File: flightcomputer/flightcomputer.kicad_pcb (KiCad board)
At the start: 2 copper layers, 112 x 120 mm, 0 parts

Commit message: all boards
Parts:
- added BZ1: Buzzer, Buzzer_Beeper:MagneticBuzzer_PUI_AT-0927-TT-6-R, F.Cu at (162.8, 84.8)
- added C1: 0.1uF, Capacitor_SMD:C_0402_1005Metric_Pad0.74x0.62mm_HandSolder, F.Cu at (152.9, 93.3)
- added C10: 10uF, Capacitor_SMD:C_0603_1608Metric_Pad1.08x0.95mm_HandSolder, F.Cu at (163.2, 134.0)
- added C11: 10uF, Capacitor_SMD:C_0603_1608Metric_Pad1.08x0.95mm_HandSolder, F.Cu at (137.9, 98.0)
- added C2: 220nF, Capacitor_SMD:C_0402_1005Metric_Pad0.74x0.62mm_HandSolder, F.Cu at (152.9, 95.2)
- added C3: 0.1uF, Capacitor_SMD:C_0402_1005Metric_Pad0.74x0.62mm_HandSolder, F.Cu at (152.9, 97.2)
- added C4: 100nF, Capacitor_SMD:C_0402_1005Metric_Pad0.74x0.62mm_HandSolder, F.Cu at (152.9, 99.2)
- added C5: 0.1uF, Capacitor_SMD:C_0402_1005Metric_Pad0.74x0.62mm_HandSolder, F.Cu at (152.9, 101.2)
- added C6: 10uF, Capacitor_SMD:C_0402_1005Metric_Pad0.74x0.62mm_HandSolder, F.Cu at (152.9, 103.1)
- added C7: 10uF, Capacitor_SMD:C_0603_1608Metric_Pad1.08x0.95mm_HandSolder, F.Cu at (137.9, 90.5)
- added C8: 22uF, Capacitor_SMD:C_0603_1608Metric_Pad1.08x0.95mm_HandSolder, F.Cu at (137.9, 93.0)
- added C9: 100nF, Capacitor_SMD:C_0603_1608Metric_Pad1.08x0.95mm_HandSolder, F.Cu at (137.9, 95.5)
- added D1: LED, LED_SMD:LED_0603_1608Metric_Pad1.05x0.95mm_HandSolder, F.Cu at (171.6, 91.4)
- added D2: LED, LED_SMD:LED_0603_1608Metric_Pad1.05x0.95mm_HandSolder, F.Cu at (171.6, 94.0)
- added D3: LED, LED_SMD:LED_0603_1608Metric_Pad1.05x0.95mm_HandSolder, F.Cu at (171.6, 96.6)
- added H1: MountingHole_Pad, MountingHole:MountingHole_2.2mm_M2_DIN965_Pad, F.Cu at (113.6, 82.2)
- added H2: MountingHole_Pad, MountingHole:MountingHole_2.2mm_M2_DIN965_Pad, F.Cu at (113.6, 87.6)
- added H3: MountingHole_Pad, MountingHole:MountingHole_2.2mm_M2_DIN965_Pad, F.Cu at (113.6, 92.9)
- added H4: MountingHole_Pad, MountingHole:MountingHole_2.2mm_M2_DIN965_Pad, F.Cu at (113.6, 98.3)
- added J1: Conn_Coaxial, Connector_Coaxial:U.FL_Hirose_U.FL-R-SMT-1_Vertical, F.Cu at (163.6, 143.3)
- added J10: Conn_01x03, Connector_PinHeader_2.54mm:PinHeader_1x03_P2.54mm_Vertical, F.Cu at (135.0, 81.9)
- added J11: Conn_01x03, Connector_PinHeader_2.54mm:PinHeader_1x03_P2.54mm_Vertical, F.Cu at (139.6, 81.9)
- added J12: 282837-2, HPRfootprints:TE_282837-2, F.Cu at (122.2, 84.4)
- added J13: 282837-2, HPRfootprints:TE_282837-2, F.Cu at (122.2, 94.2)
- added J2: Conn_Coaxial, Connector_Coaxial:SMA_Amphenol_132134-10_Vertical, F.Cu at (143.6, 119.8)
- added J3: Conn_Coaxial, Connector_Coaxial:U.FL_Hirose_U.FL-R-SMT-1_Vertical, F.Cu at (169.0, 143.3)
- added J4: Conn_Coaxial, Connector_Coaxial:SMA_Amphenol_132134-10_Vertical, F.Cu at (143.6, 129.0)
- added J5: Conn_01x24, Connector_Molex:Molex_SL_171971-0024_1x24_P2.54mm_Vertical, F.Cu at (3.02, 3.08)
- added J6: Conn_01x24, Connector_Molex:Molex_SL_171971-0024_1x24_P2.54mm_Vertical, F.Cu at (3.02, 11.7)
- added J7: Conn_01x01, Connector_PinHeader_2.54mm:PinHeader_1x01_P2.54mm_Vertical, F.Cu at (130.3, 81.9)
- added J8: Conn_01x01, Connector_PinHeader_2.54mm:PinHeader_1x01_P2.54mm_Vertical, F.Cu at (130.3, 86.5)
- added J9: Conn_01x02, Connector_JST:JST_PH_S2B-PH-K_1x02_P2.00mm_Horizontal, F.Cu at (162.5, 100.8)
- added M1: Motor_Servo, Connector_PinHeader_2.54mm:PinHeader_1x03_P2.54mm_Vertical, F.Cu at (144.3, 81.9)
- added M2: Motor_Servo, Connector_PinHeader_2.54mm:PinHeader_1x03_P2.54mm_Vertical, F.Cu at (148.9, 81.9)
- added Q1: MMBT3904, Package_TO_SOT_SMD:SOT-23, F.Cu at (172.5, 81.9)
- added Q2: MMBT3904, Package_TO_SOT_SMD:SOT-23, F.Cu at (172.5, 86.6)
- added Q3: SI4925DDY-T1-GE3, HPRfootprints:SOIC127P600X175-8N, F.Cu at (120.5, 102.3)
- added R1: 4.7k, Resistor_SMD:R_0603_1608Metric_Pad0.98x0.95mm_HandSolder, F.Cu at (163.2, 136.5)
- added R10: 150, Resistor_SMD:R_0603_1608Metric_Pad0.98x0.95mm_HandSolder, F.Cu at (146.6, 93.0)
- added R11: 150, Resistor_SMD:R_0603_1608Metric_Pad0.98x0.95mm_HandSolder, F.Cu at (146.6, 95.5)
- added R2: 4.7k, Resistor_SMD:R_0603_1608Metric_Pad0.98x0.95mm_HandSolder, F.Cu at (163.2, 139.0)
- added R3: 1.2k, Resistor_SMD:R_0603_1608Metric_Pad0.98x0.95mm_HandSolder, F.Cu at (137.9, 100.5)
- added R4: 4.7k, Resistor_SMD:R_0603_1608Metric_Pad0.98x0.95mm_HandSolder, F.Cu at (142.2, 90.5)
- added R5: 1K, Resistor_SMD:R_0603_1608Metric_Pad0.98x0.95mm_HandSolder, F.Cu at (142.2, 93.0)
- added R6: 1K, Resistor_SMD:R_0603_1608Metric_Pad0.98x0.95mm_HandSolder, F.Cu at (142.2, 95.5)
- added R7: 10K, Resistor_SMD:R_0603_1608Metric_Pad0.98x0.95mm_HandSolder, F.Cu at (142.2, 98.0)
- added R8: 10K, Resistor_SMD:R_0603_1608Metric_Pad0.98x0.95mm_HandSolder, F.Cu at (142.2, 100.5)
- added R9: 150, Resistor_SMD:R_0603_1608Metric_Pad0.98x0.95mm_HandSolder, F.Cu at (146.6, 90.5)
- added S1: KMR221GLFS, HPRfootprints:SW_KMR221GLFS, F.Cu at (170.7, 100.9)
- added S2: KMR221GLFS, HPRfootprints:SW_KMR221GLFS, F.Cu at (170.7, 105.5)
- added TP1: TestPoint, Connector_PinHeader_2.54mm:PinHeader_1x01_P2.54mm_Vertical, F.Cu at (130.3, 91.2)
- added TP2: TestPoint, Connector_PinHeader_2.54mm:PinHeader_1x01_P2.54mm_Vertical, F.Cu at (130.3, 95.8)
- added TP3: TestPoint, TestPoint:TestPoint_Pad_1.0x1.0mm, F.Cu at (134.2, 90.8)
- added TP4: TestPoint, TestPoint:TestPoint_Pad_1.0x1.0mm, F.Cu at (134.2, 93.8)
- added TP5: TestPoint, TestPoint:TestPoint_Pad_1.0x1.0mm, F.Cu at (134.2, 96.9)
- added TP6: TestPoint, TestPoint:TestPoint_Pad_1.0x1.0mm, F.Cu at (134.2, 99.9)
- added TP7: TestPoint, TestPoint:TestPoint_Pad_1.0x1.0mm, F.Cu at (134.2, 103.0)
- added U1: MAX-M10S, RF_GPS:ublox_MAX, F.Cu at (154.7, 138.7)
- added U2: LIS2MDLTR, HPRfootprints:PQFN50P200X200X70-12N, F.Cu at (144.2, 103.6)
- added U3: BMI088, HPRfootprints:PQFN50P450X300X100-16N, F.Cu at (138.9, 104.6)
- added U4: MS5607-02BA, Package_LGA:LGA-8_3x5mm_P1.25mm, F.Cu at (156.9, 95.8)
- added U5: MIC29302AWD-TR, HPRfootprints:TO-252-5_MCH, F.Cu at (155.4, 85.2)
- added U6: RFM95W-915S2, RF_Module:HOPERF_RFM9XW_SMD, F.Cu at (158.0, 124.0)
- added U7: Teensy4.1, HPRfootprints:Teensy41, F.Cu at (147.5, 64.5)
- added U8: LD1117S50TR_SOT223, Package_TO_SOT_SMD:SOT-223-3_TabPin2, F.Cu at (164.4, 94.3)

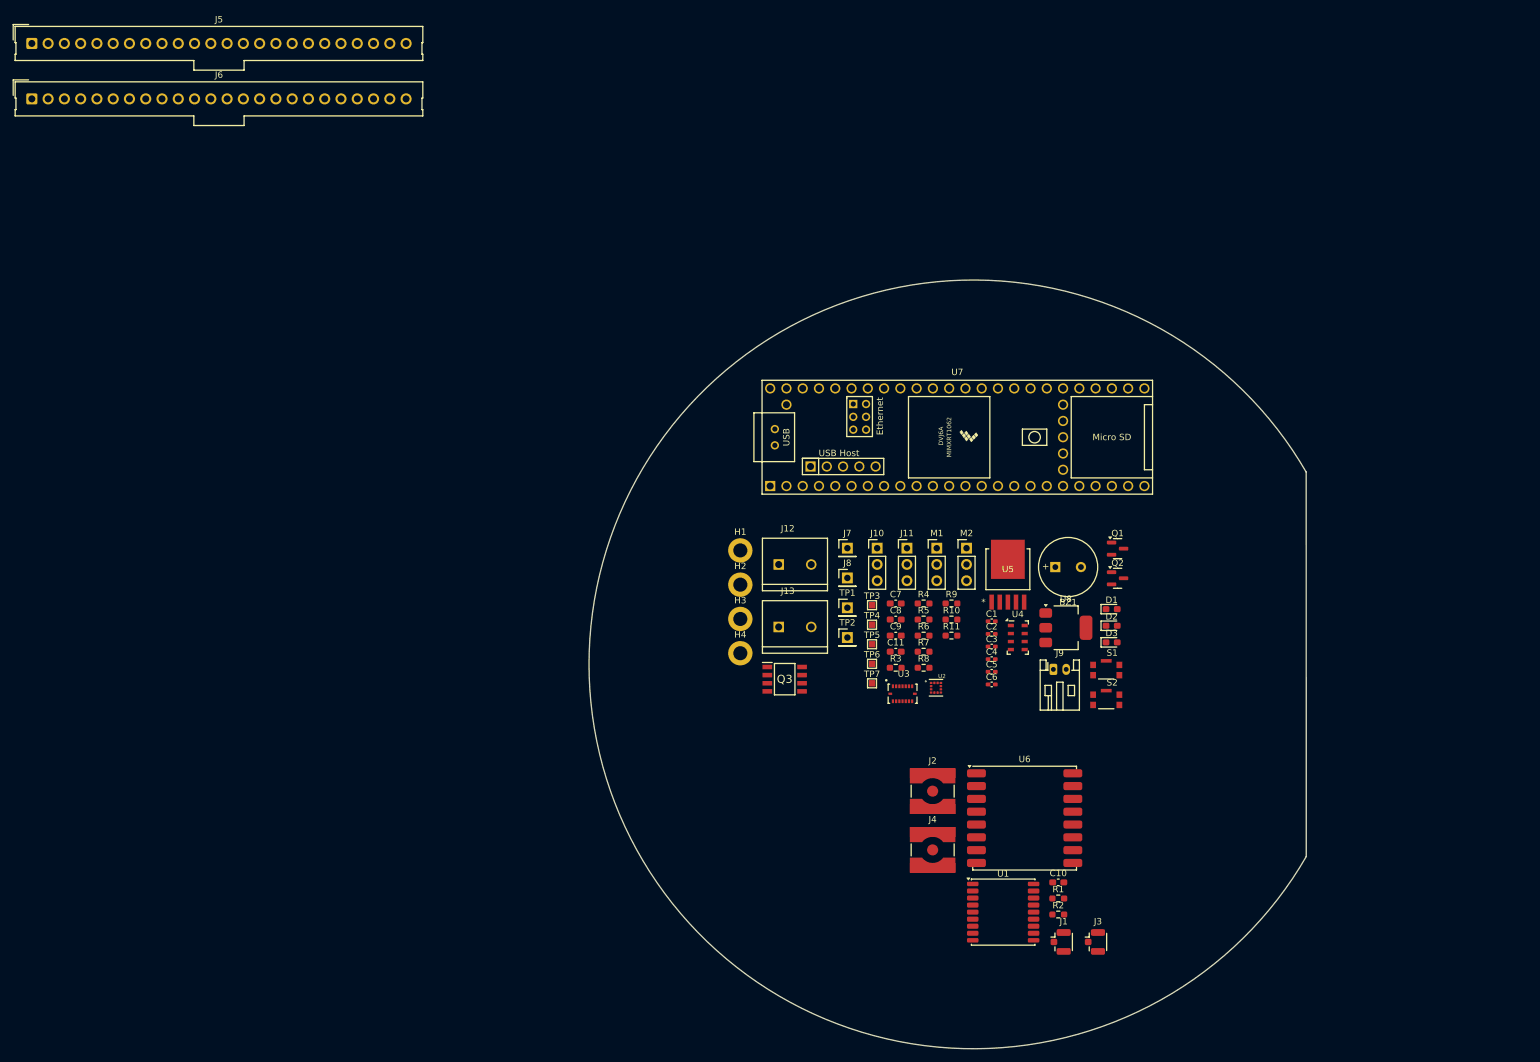
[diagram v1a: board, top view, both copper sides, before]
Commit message: no esp32, may add
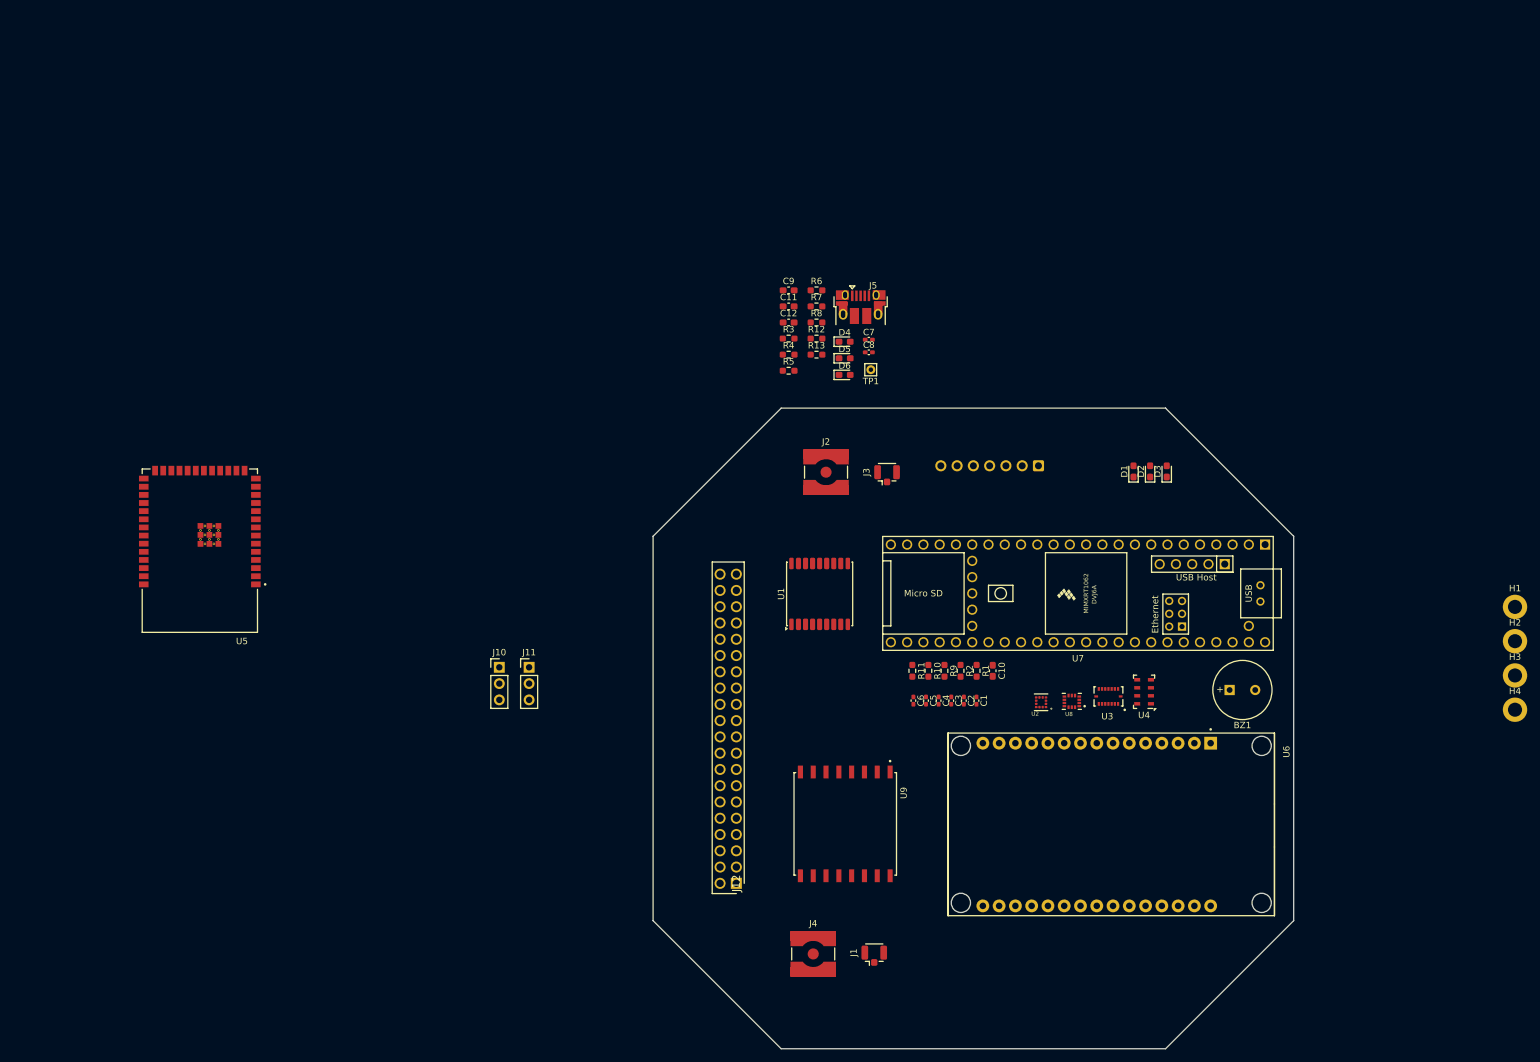
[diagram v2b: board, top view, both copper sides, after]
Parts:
- removed J6: Conn_01x24, Connector_Molex:Molex_SL_171971-0024_1x24_P2.54mm_Vertical
- removed J7, J8: Conn_01x01, Connector_PinHeader_2.54mm:PinHeader_1x01_P2.54mm_Vertical
- removed J9: Conn_01x02, Connector_JST:JST_PH_S2B-PH-K_1x02_P2.00mm_Horizontal
- removed M1, M2: Motor_Servo, Connector_PinHeader_2.54mm:PinHeader_1x03_P2.54mm_Vertical
- removed Q1, Q2: MMBT3904, Package_TO_SOT_SMD:SOT-23
- removed Q3: SI4925DDY-T1-GE3, HPRfootprints:SOIC127P600X175-8N
- removed S1, S2: KMR221GLFS, HPRfootprints:SW_KMR221GLFS
- removed TP2: TestPoint, Connector_PinHeader_2.54mm:PinHeader_1x01_P2.54mm_Vertical
- removed TP3, TP4, TP5, TP6, TP7: TestPoint, TestPoint:TestPoint_Pad_1.0x1.0mm
- added C12: 1uF, Capacitor_SMD:C_0603_1608Metric_Pad1.08x0.95mm_HandSolder, F.Cu at (121.2, 46.6)
- added D4: LED, LED_SMD:LED_0603_1608Metric_Pad1.05x0.95mm_HandSolder, F.Cu at (129.9, 49.6)
- added D5: LED, LED_SMD:LED_0603_1608Metric_Pad1.05x0.95mm_HandSolder, F.Cu at (129.9, 52.2)
- added D6: LED, LED_SMD:LED_0603_1608Metric_Pad1.05x0.95mm_HandSolder, F.Cu at (129.9, 54.8)
- added R12: 500, Resistor_SMD:R_0603_1608Metric_Pad0.98x0.95mm_HandSolder, F.Cu at (125.5, 49.1)
- added R13: 500, Resistor_SMD:R_0603_1608Metric_Pad0.98x0.95mm_HandSolder, F.Cu at (125.5, 51.6)
- added U9: RFM96W-433S2, HPRfootprints:MODULE_RFM96W-433S2, F.Cu at (130.0, 124.9)
- C11: value 10uF -> 0.1uF
- C7: value 10uF -> 100nF; footprint Capacitor_SMD:C_0603_1608Metric_Pad1.08x0.95mm_HandSolder -> Capacitor_SMD:C_0402_1005Metric_Pad0.74x0.62mm_HandSolder
- C8: value 22uF -> 100nF; footprint Capacitor_SMD:C_0603_1608Metric_Pad1.08x0.95mm_HandSolder -> Capacitor_SMD:C_0402_1005Metric_Pad0.74x0.62mm_HandSolder
- C9: value 100nF -> 0.1uF
- J12: value 282837-2 -> M20-6102045; footprint HPRfootprints:TE_282837-2 -> HPRfootprints:RHDR40W66P254_2X20_5146X500X1105P
- J13: value 282837-2 -> Conn_01x07; footprint HPRfootprints:TE_282837-2 -> Connector_Molex:Molex_SL_171971-0007_1x07_P2.54mm_Vertical; moved to B.Cu
- J5: value Conn_01x24 -> USB_B_Micro; footprint Connector_Molex:Molex_SL_171971-0024_1x24_P2.54mm_Vertical -> Connector_USB:USB_Micro-B_Amphenol_10103594-0001LF_Horizontal
- R10, R11, R9: value 150 -> 500
- R3: value 1.2k -> 0
- R4: value 4.7k -> 0
- R5, R6: value 1K -> 0
- R7: value 10K -> 10k
- R8: value 10K -> 500
- TP1: footprint Connector_PinHeader_2.54mm:PinHeader_1x01_P2.54mm_Vertical -> Connector_Pin:Pin_D0.7mm_L6.5mm_W1.8mm_FlatFork
- U5: value MIC29302AWD-TR -> ESP32-S3-WROOM-1-N4; footprint HPRfootprints:TO-252-5_MCH -> HPRfootprints:XCVR_ESP32-S3-WROOM-1-N4
- U6: value RFM95W-915S2 -> ESP32-DEVKIT-V1; footprint RF_Module:HOPERF_RFM9XW_SMD -> HPRfootprints:MODULE_ESP32_DEVKIT_V1
- U8: value LD1117S50TR_SOT223 -> LSM6DSO32TR; footprint Package_TO_SOT_SMD:SOT-223-3_TabPin2 -> HPRfootprints:XDCR_LSM6DSO32TR
- moved J5 135.8 mm to (132.4, 44.2)
- moved U5 126.2 mm to (29.2, 82.2), turned to 180 degrees
- moved H1 121.3 mm to (234.6, 91.0)
- moved H2 121.3 mm to (234.6, 96.4)
- moved H3 121.3 mm to (234.6, 101.7)
- moved H4 121.3 mm to (234.6, 107.1)
- moved J3 79.8 mm to (136.5, 70.5), turned to 90 degrees
- moved J10 61.8 mm to (76.0, 100.5)
- moved J11 61.8 mm to (80.7, 100.5)
- moved U1 57.3 mm to (126.0, 89.0), turned to 90 degrees
- moved C11 56.4 mm to (121.2, 44.1)
- moved R7 56.4 mm to (125.5, 44.1)
- moved C9 56.4 mm to (121.2, 41.6)
- moved R6 56.4 mm to (125.5, 41.6)
- moved R8 56.4 mm to (125.5, 46.6)
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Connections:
- C11 pad 1: /ldo_5v -> GND
- C11 pad 2: GND -> /esp_pu
- C7 pad 1: /VBATT -> Net-(U8-VDDIO)
- C8 pad 1: /ldo_6v -> Net-(U8-VDD)
- C9 pad 1: /VBATT -> GND
- C9 pad 2: GND -> /esp_boot
- J12 pad 1: Net-(Q3-D1_1) -> unconnected-(J12-Pad1)
- J12 pad 2: GND -> unconnected-(J12-Pad2)
- J13 pad 1: Net-(Q3-D2_1) -> /sd_cs
- J13 pad 2: GND -> /sd_mosi
- J5 pad 1: GND -> unconnected-(J5-VBUS-Pad1)
- J5 pad 2: /radio_reset -> unconnected-(J5-D--Pad2)
- J5 pad 3: /radio_miso -> unconnected-(J5-D+-Pad3)
- J5 pad 4: /LED3 -> unconnected-(J5-ID-Pad4)
- J5 pad 5: /LED2 -> unconnected-(J5-GND-Pad5)
- J5 pad 6: /LED1 -> unconnected-(J5-Shield-Pad6)
- R3 pad 1: Net-(U5-ADJ) -> /radio_cs
- R3 pad 2: GND -> /sd_cs
- R4 pad 1: Net-(U5-ADJ) -> /radio_mosi
- R4 pad 2: /ldo_6v -> /sd_mosi
- R5 pad 1: /PYRO1 -> /radio_miso
- R5 pad 2: Net-(Q1-B) -> /sd_miso
- R6 pad 1: /PYRO2 -> /radio_sck
- R6 pad 2: Net-(Q2-B) -> /sd_sck
- R7 pad 1: /VBATT -> /esp_pu
- R7 pad 2: Net-(Q1-C) -> unconnected-(R7-Pad2)
- R8 pad 1: /VBATT -> /LED4
- TP1 pad 1: /ldo_6v -> Net-(U7-VUSB)
- U5 pad 1: /VBATT -> GND
- U5 pad 2: /VBATT -> unconnected-(U5-3V3-Pad2)
- U5 pad 3: GND -> unconnected-(U5-EN-Pad3)
- U5 pad 4: /ldo_6v -> unconnected-(U5-IO4-Pad4)
- U5 pad 5: Net-(U5-ADJ) -> unconnected-(U5-IO5-Pad5)
- U5 pad 6: GND -> unconnected-(U5-IO6-Pad6)
- U6 pad 1: GND -> unconnected-(U6-3V3-Pad1)
- U6 pad 10: GND -> unconnected-(U6-D19-Pad10)
- U6 pad 11: /radio_dio3 -> unconnected-(U6-D21-Pad11)
- U6 pad 12: /radio_dio4 -> unconnected-(U6-RX0-Pad12)
- U6 pad 13: /teensy_3.3v -> unconnected-(U6-TX0-Pad13)
- U6 pad 14: /radio_dio0 -> unconnected-(U6-D22-Pad14)
- U6 pad 15: /radio_dio1 -> unconnected-(U6-D23-Pad15)
- U6 pad 16: /radio_dio2 -> unconnected-(U6-EN-Pad16)
- U6 pad 2: /radio_miso -> Net-(U6-GND-Pad2)
- U6 pad 3: /radio_mosi -> unconnected-(U6-D15-Pad3)
- U6 pad 4: /radio_sck -> unconnected-(U6-D2-Pad4)
- U6 pad 5: /radio_cs -> unconnected-(U6-D4-Pad5)
- U6 pad 6: /radio_reset -> unconnected-(U6-RX2-Pad6)
- U6 pad 7: /radio_dio5 -> unconnected-(U6-TX2-Pad7)
- U6 pad 8: GND -> unconnected-(U6-D5-Pad8)
- U6 pad 9: Net-(J3-In) -> unconnected-(U6-D18-Pad9)
- U7 pad 18: /radio_mosi -> unconnected-(U7-26_A12_MOSI1-Pad18)
- U7 pad 19: /radio_sck -> unconnected-(U7-27_A13_SCK1-Pad19)
- U7 pad 2: /radio_reset -> unconnected-(U7-0_RX1_CRX2_CS1-Pad2)
- U7 pad 20: /radio_cs -> unconnected-(U7-28_RX7-Pad20)
- U7 pad 21: /radio_dio0 -> unconnected-(U7-29_TX7-Pad21)
- U7 pad 22: /radio_dio1 -> unconnected-(U7-30_CRX3-Pad22)
- U7 pad 23: /radio_dio2 -> unconnected-(U7-31_CTX3-Pad23)
- U7 pad 24: /radio_dio5 -> unconnected-(U7-32_OUT1B-Pad24)
- U7 pad 25: /buzz_pwm -> unconnected-(U7-33_MCLK2-Pad25)
- U7 pad 3: /radio_miso -> unconnected-(U7-1_TX1_CTX2_MISO1-Pad3)
- U7 pad 40: /GPS_sda -> unconnected-(U7-18_A4_SDA-Pad40)
- U7 pad 41: /GPS_scl -> unconnected-(U7-19_A5_SCL-Pad41)
- U7 pad 42: /GPS_reset -> unconnected-(U7-20_A6_TX5_LRCLK1-Pad42)
- U7 pad 43: /GPS_int -> unconnected-(U7-21_A7_RX5_BCLK1-Pad43)
- U7 pad 48: /ldo_5v -> /5V
- U7 pad 49: unconnected-(U7-VUSB-Pad49) -> Net-(U7-VUSB)
- U7 pad 53: Net-(U7-PROGRAM) -> unconnected-(U7-PROGRAM-Pad53)
- U8 pad 1: GND -> /SENSE_miso
- U8 pad 2: /ldo_5v -> GND
- U8 pad 3: /VBATT -> GND
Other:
- board size 112 x 120 mm -> 100 x 100 mm

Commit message: gps and radio additions
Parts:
- removed C11, C9: 0.1uF, Capacitor_SMD:C_0603_1608Metric_Pad1.08x0.95mm_HandSolder
- removed C12: 1uF, Capacitor_SMD:C_0603_1608Metric_Pad1.08x0.95mm_HandSolder
- removed J5: USB_B_Micro, Connector_USB:USB_Micro-B_Amphenol_10103594-0001LF_Horizontal
- removed R7: 10k, Resistor_SMD:R_0603_1608Metric_Pad0.98x0.95mm_HandSolder
- removed U5: ESP32-S3-WROOM-1-N4, HPRfootprints:XCVR_ESP32-S3-WROOM-1-N4
- removed U6: ESP32-DEVKIT-V1, HPRfootprints:MODULE_ESP32_DEVKIT_V1
- J13: moved to F.Cu
- moved H3 110.7 mm to (124.5, 89.8), turned to -90 degrees
- moved H2 104.9 mm to (129.8, 89.8), turned to -90 degrees
- moved H1 99.4 mm to (135.2, 89.8), turned to -90 degrees
- moved C8 90.3 mm to (183.2, 126.8)
- moved C7 89.0 mm to (182.8, 123.5)
- moved D6 86.9 mm to (179.4, 126.3)
- moved R6 80.8 mm to (180.0, 101.3), turned to -90 degrees
- moved R12 78.5 mm to (180.0, 105.7), turned to -90 degrees
- moved R5 77.4 mm to (182.5, 101.3), turned to -90 degrees
- moved TP1 76.0 mm to (185.7, 109.8), turned to -90 degrees
- moved R8 75.5 mm to (177.5, 101.3), turned to -90 degrees
- moved R13 75.0 mm to (177.5, 105.7), turned to -90 degrees
- moved R3 72.0 mm to (175.0, 97.0), turned to -90 degrees
- moved J4 63.7 mm to (136.6, 82.5), turned to -90 degrees
- moved J10 60.8 mm to (127.0, 67.3), turned to -90 degrees
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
